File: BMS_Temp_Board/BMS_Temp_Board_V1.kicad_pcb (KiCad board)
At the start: 4 copper layers, 68 x 83.4 mm, 69 parts, among them IC1 ESP32-S3-WROOM-1-N8R8, IC2 CP2102N-A02-GQFN28, IC3 TLP175A_TPL,E, IC4 TPS2116DRLR, IC5 MIC37100-3.3WS, IC6 CD74HC4067PWR, IC7 CD74HC4067PWR, IC8 CD74HC4067PWR, IC9 CD74HC4067PWR, J1 ESP_USB, J2 B32B-PUDSS-1_LF__SN_, J3 B32B-PUDSS-1_LF__SN_, J4 B32B-PUDSS-1_LF__SN_, J5 B32B-PUDSS-1_LF__SN_, J6 776279-1, Q1 MMBT2222LT1G, Q2 MMBT2222LT1G, U1 USBLC6-2SC6, U2 SN65HVD230, U3 LM2575HVS-5.0_NOPB

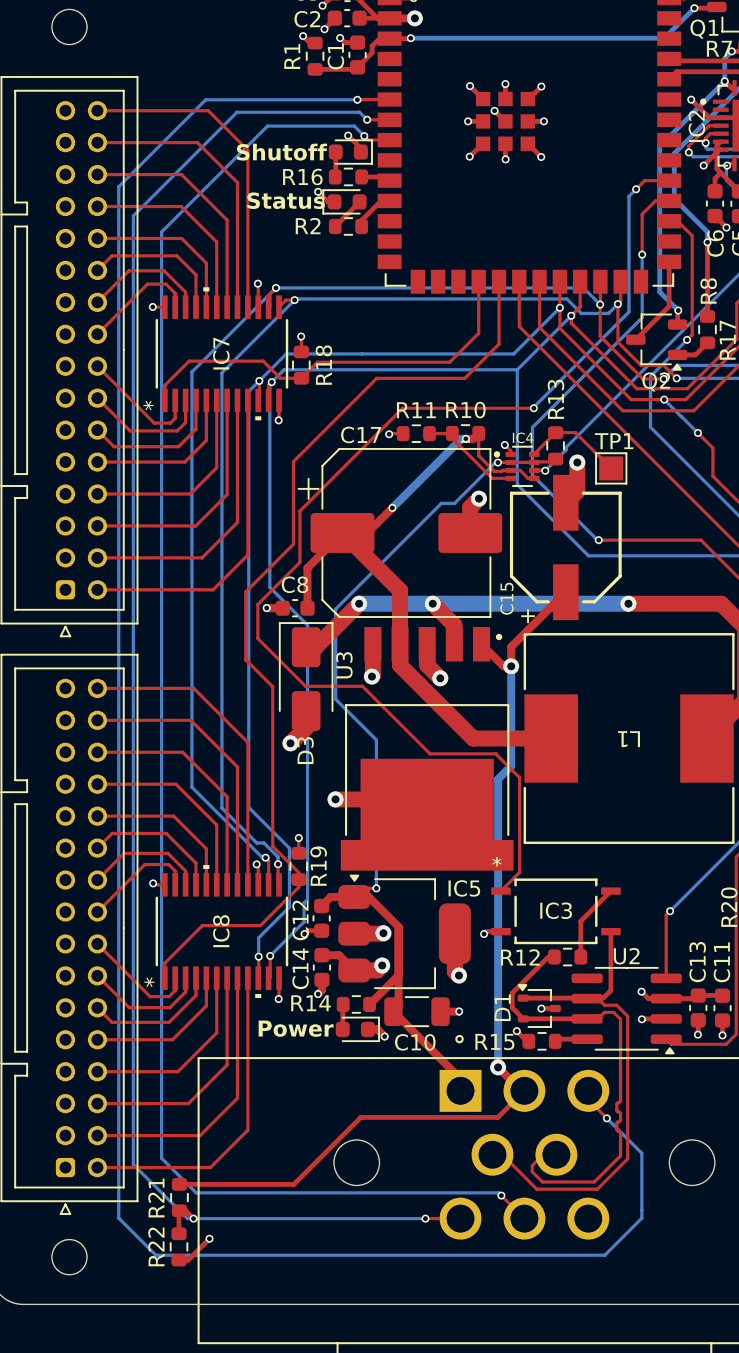
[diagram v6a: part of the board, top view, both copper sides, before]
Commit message: Added optoisolator to shutoff signal output, updated BOM
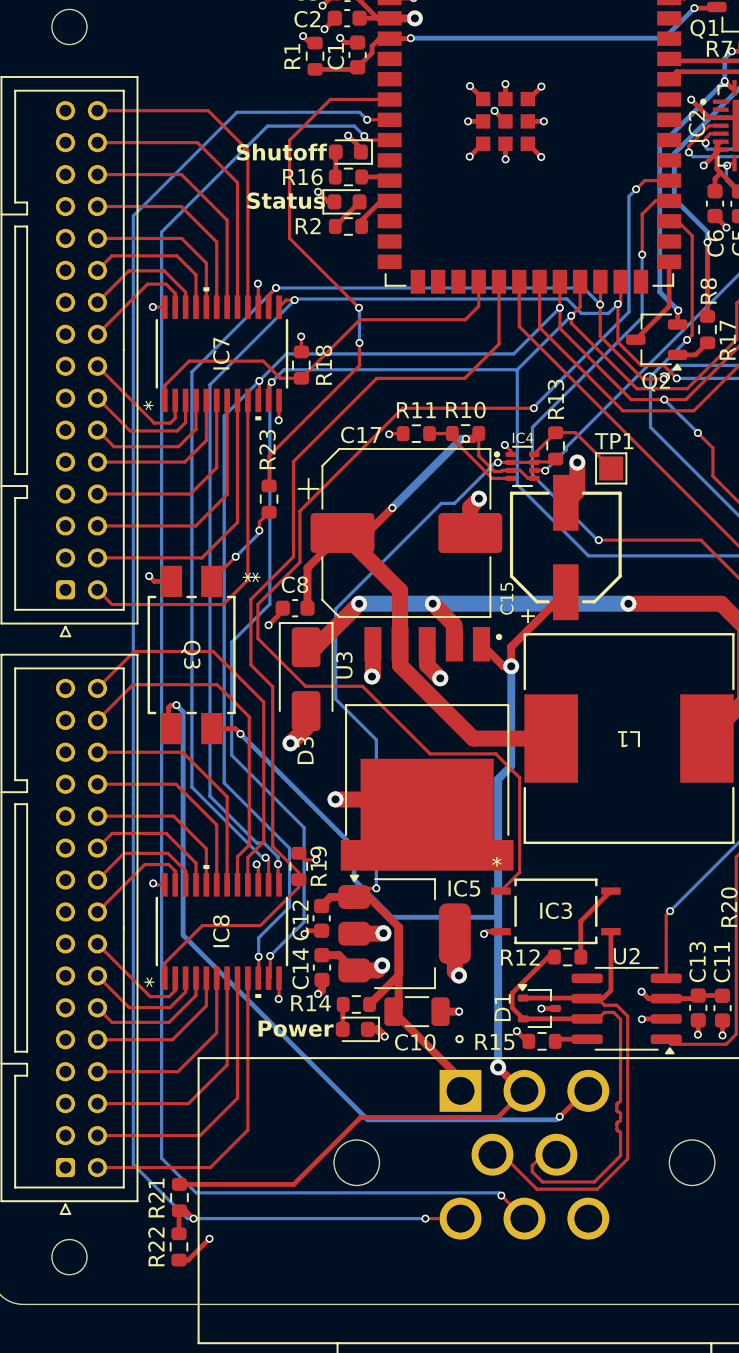
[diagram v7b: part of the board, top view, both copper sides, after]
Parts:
- added Q3: LTV-817S-TA1, LTV_817S_TA1:LTV-817S_LTO, F.Cu at (92.6, 112.5)
- added R23: 220, Resistor_SMD:R_0603_1608Metric, F.Cu at (97.4, 102.7)
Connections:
- J6 pad 3: /SHUTOFF -> /SHUTOFF_ISO
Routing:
- net /SHUTOFF: track 127.8 -> 33.1 mm
- net /SHUTOFF_ISO: track 0.00 -> 47.4 mm, vias 0 -> 2
- net +12V: track 60.2 -> 84.2 mm, vias 2 -> 3
- net Net-(Q3-Pad1): track 0.00 -> 5.81 mm, vias 0 -> 2
- net Net-(IC8-I15): track 19.7 -> 24.5 mm
- net Net-(IC8-I14): track 17.4 -> 22.1 mm
- net GND: track 84.7 -> 87.0 mm, vias 59 -> 60
- net /MUX_S1: track 130.4 -> 132.2 mm
- net Net-(IC7-I0): track 20.0 -> 21.7 mm
- net /MUX_S0: track 117.6 -> 118.9 mm
- net /MUX2: track 26.1 -> 25.1 mm
- net /MUX_S3: track 115.8 -> 116.5 mm
